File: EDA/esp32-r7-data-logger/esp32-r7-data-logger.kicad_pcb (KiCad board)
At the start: 2 copper layers, 25.6 x 22.4 mm, 2 parts, among them U1 ESP32-WROOM-32U

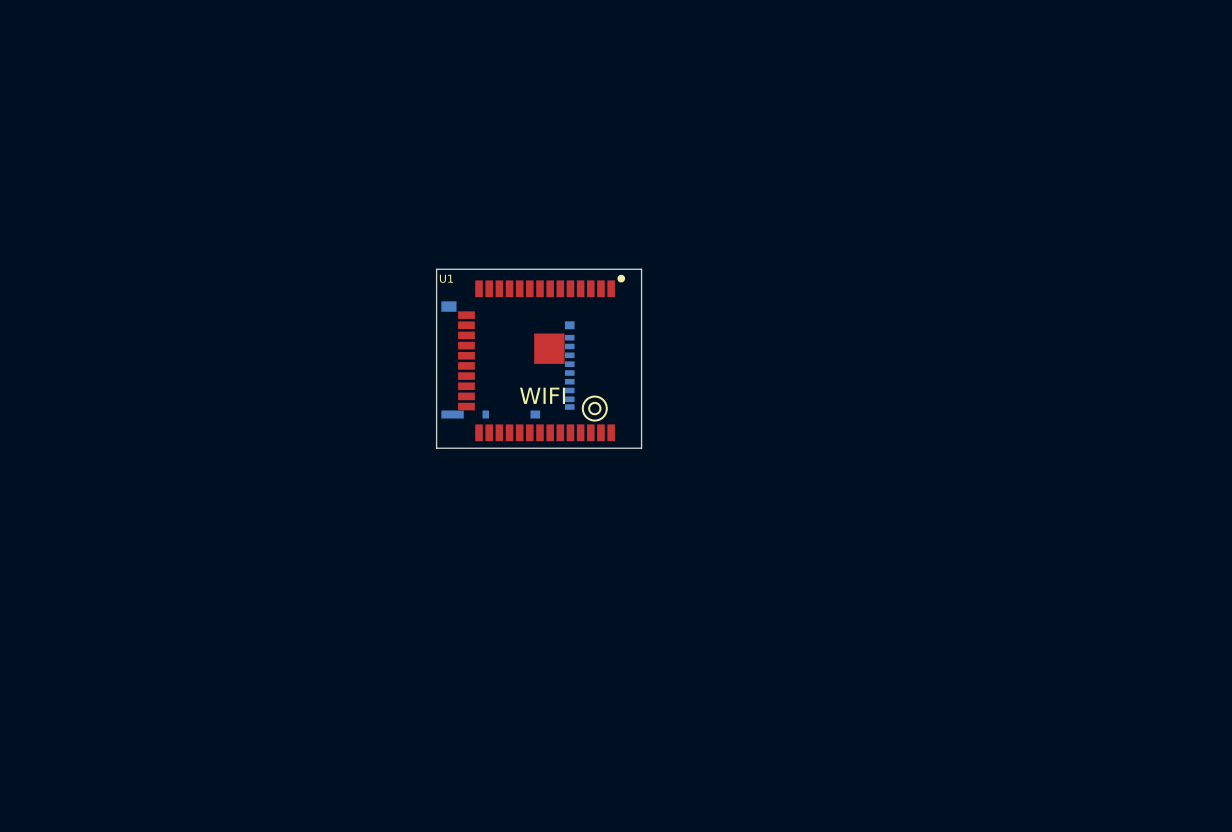
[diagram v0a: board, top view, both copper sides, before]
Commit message: Updates to EDA files for symbols that don't throw errors during ERC
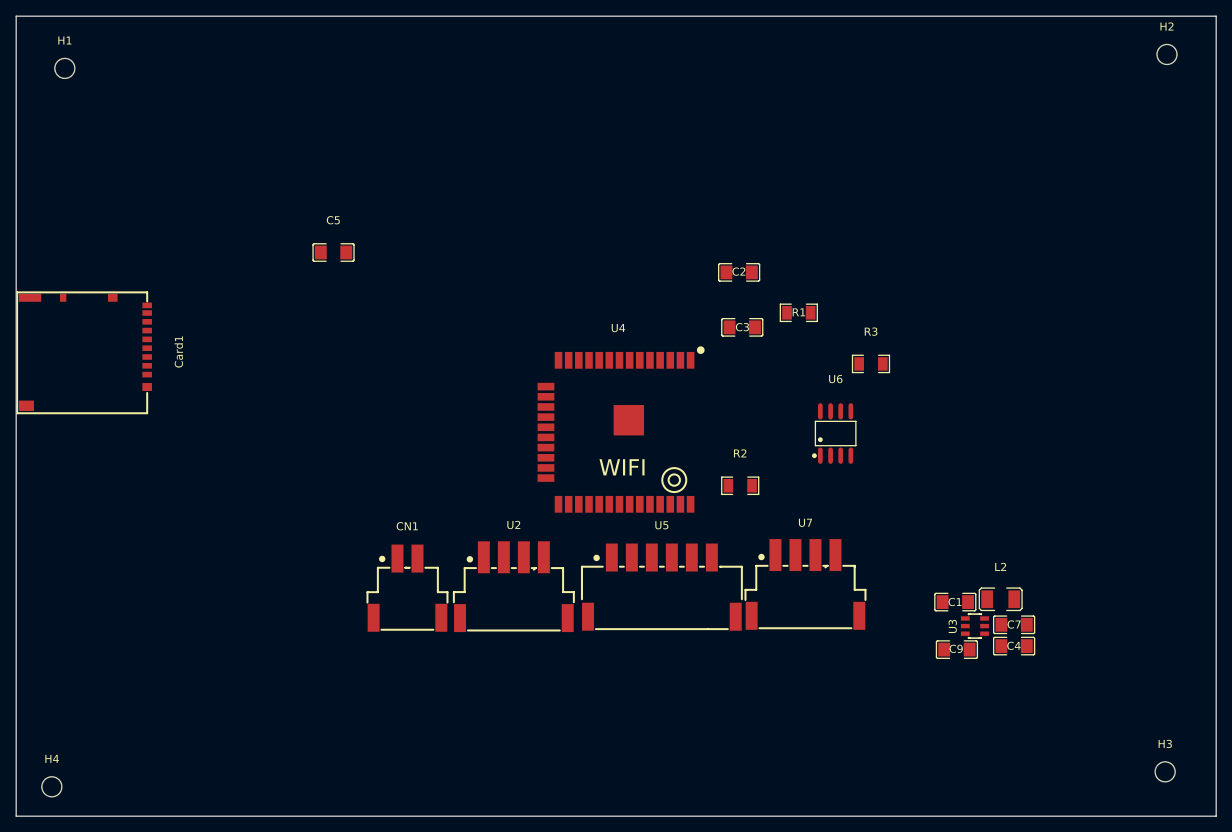
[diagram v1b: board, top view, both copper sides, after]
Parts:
- removed U1: ESP32-WROOM-32U, easyeda2kicad:WIFIM-SMD_38P-L19.2-W18.0-P1.27
- added C1: 10uF, easyeda2kicad:C1206, F.Cu at (180.6, 117.9)
- added C2: 22uF, easyeda2kicad:C1206, F.Cu at (153.6, 76.7)
- added C3: 10uF, easyeda2kicad:C1206, F.Cu at (154.0, 83.6)
- added C4: 22uF, easyeda2kicad:C1206, F.Cu at (188.0, 123.4)
- added C5: 10uF, easyeda2kicad:C1206, F.Cu at (102.9, 74.2)
- added C7: 22uF, easyeda2kicad:C1206, F.Cu at (188.0, 120.8)
- added C9: 100nF, easyeda2kicad:C1206, F.Cu at (180.8, 123.9)
- added CN1: ZX-XH2.54-2PWT, easyeda2kicad:CONN-SMD_2P-P2.54_MEGASTAR_ZX-XH2.54-2PWT, F.Cu at (112.2, 116.2)
- added H1: MountingHole, MountingHole:MountingHole_2.5mm, F.Cu at (69.3, 51.2)
- added H2: MountingHole, MountingHole:MountingHole_2.5mm, F.Cu at (207.1, 49.5)
- added H3: MountingHole, MountingHole:MountingHole_2.5mm, F.Cu at (206.9, 139.2)
- added H4: MountingHole, MountingHole:MountingHole_2.5mm, F.Cu at (67.7, 141.0)
- added L2: 3.9uH, easyeda2kicad:L1210, F.Cu at (186.3, 117.6)
- added R1: 10k, easyeda2kicad:R1206, F.Cu at (161.1, 81.8)
- added R2: 3.3k, easyeda2kicad:R1206, F.Cu at (153.8, 103.4)
- added R3: 10k, easyeda2kicad:R1206, F.Cu at (170.1, 88.2)
- added U2: ZX-XH2.54-4PWT, easyeda2kicad:CONN-SMD_4P-P2.50-WAFER-254W-4P, F.Cu at (125.5, 116.1)
- added U3: AP63203WU-7, easyeda2kicad:TSOT-26_L2.9-W1.6-P0.95-LS2.8-BL, F.Cu at (183.1, 120.9)
- added U4: ESP32-WROOM-32UE, easyeda2kicad:WIFIM-SMD_38P-L19.2-W18.0-P1.27, F.Cu at (138.5, 96.7)
- added U5: ZX-XH2.54-6PWT, easyeda2kicad:CONN-SMD_ZX-XH2.54-6PWT, F.Cu at (144.0, 116.1)
- added U6: SN65HVD230DR, easyeda2kicad:SOIC-8_L4.9-W3.9-P1.27-LS6.0-BL, F.Cu at (165.7, 96.9)
- added U7: ZX-XH2.54-4PWT, easyeda2kicad:CONN-SMD_4P-P2.50-WAFER-254W-4P, F.Cu at (161.9, 115.9)
- Card1: moved to F.Cu
- moved Card1 52.8 mm to (72.1, 86.7), turned to -90 degrees
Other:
- board size 25.6 x 22.4 mm -> 150 x 100 mm
